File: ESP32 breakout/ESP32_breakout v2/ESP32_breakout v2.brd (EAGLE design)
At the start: 53.3 x 63.5 mm, 35 parts, among them U1 ESP-WROOM-32, U2 NCP-1117, Y1 12MHz

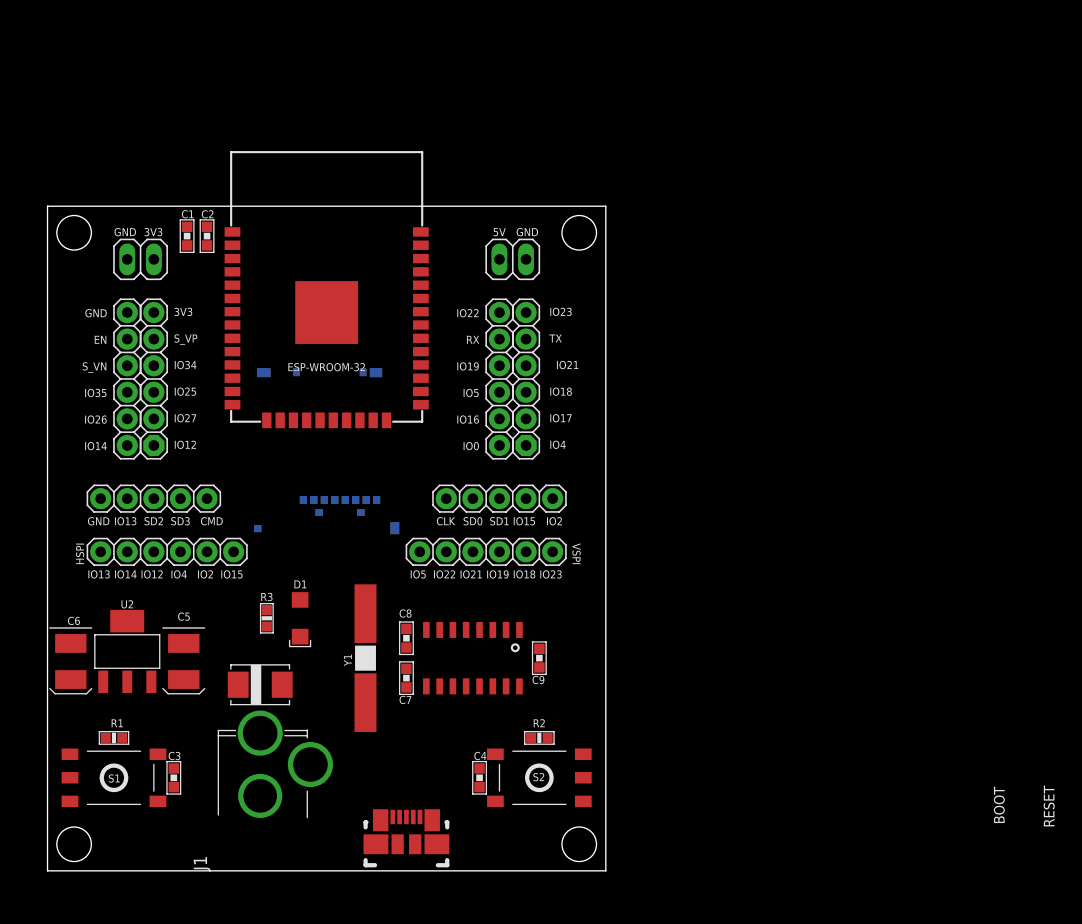
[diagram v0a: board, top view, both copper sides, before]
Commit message: Made rounded board. Modified component libraries
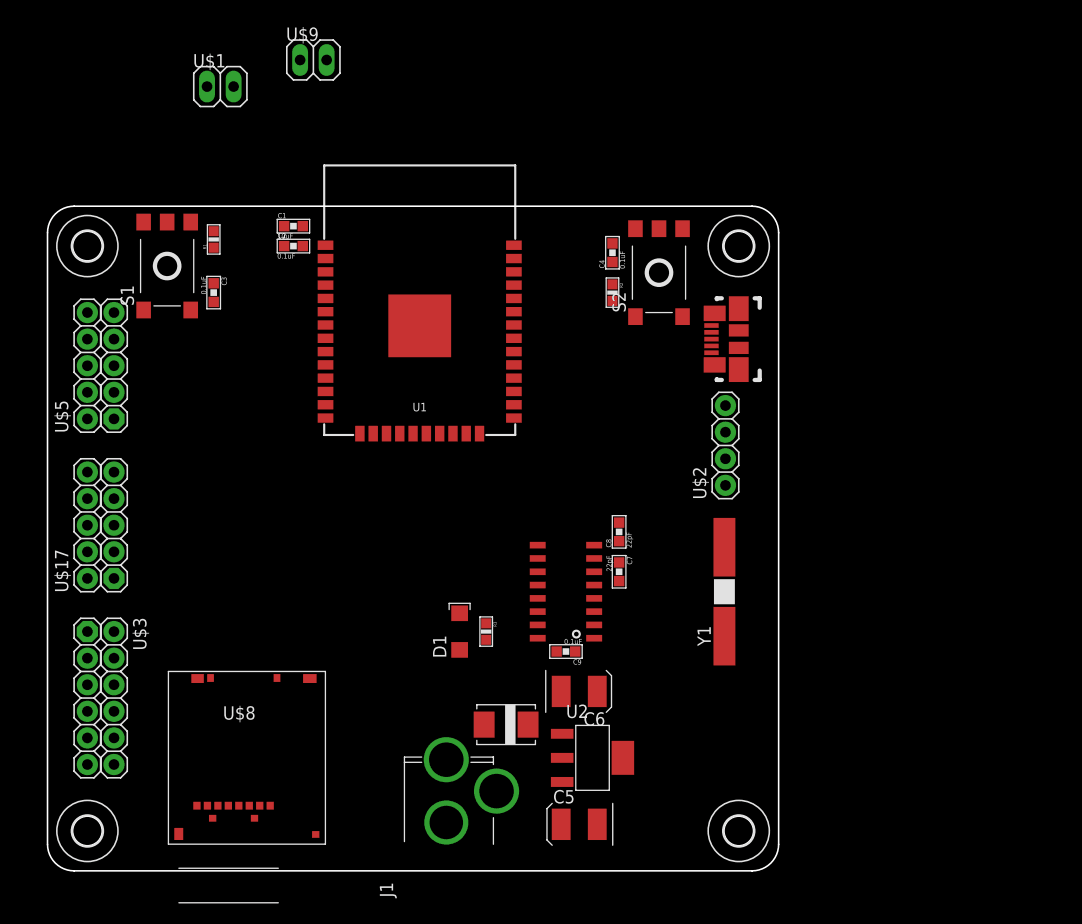
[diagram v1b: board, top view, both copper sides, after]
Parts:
- removed U$14, U$15: M05, dr-library:1X05
- removed U$6: M06, dr-library:1X06
- added U$17: M102X05, dr-library:2X05
- U$10, U$11, U$12, U$13: device EmbeddedAdventures 3:STAND-OFF-HOLE -> holes:2,8
- U$2: value M122ROWS -> M04; device dr-library:2X06 -> dr-library:1X04
- U$5: value M06 -> M102X05; device dr-library:1X06 -> dr-library:2X05
- moved U$13 85.4 mm to (66.0, 3.81)
- moved U$11 74.0 mm to (3.81, 59.7)
- moved U$4 57.8 mm to (66.0, 50.8), turned to 180 degrees
- moved U$2 57.3 mm to (64.8, 38.1)
- moved C4 51.7 mm to (54.0, 59.1)
- moved S2 49.6 mm to (58.4, 57.1), turned to 90 degrees
- moved S1 49.2 mm to (11.4, 57.8), turned to 90 degrees
- moved C6 48.7 mm to (50.8, 17.1), turned to 180 degrees
- moved R1 48.6 mm to (15.9, 60.3), turned to 90 degrees
- moved C3 46.5 mm to (15.9, 55.2)
- moved U2 45.6 mm to (52.1, 10.8), turned to 270 degrees
- moved R2 43.1 mm to (54.0, 55.2), turned to 270 degrees
- moved U$3 42.1 mm to (6.35, 21.6), turned to 270 degrees
- moved C5 40.9 mm to (50.8, 4.45), turned to 0 degrees
- moved U$5 35.9 mm to (3.81, 44.5), turned to 90 degrees
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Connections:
- net +3V3: now also U$2.4; no longer U$2.11
- net CLK: now also U$17.5; no longer U$14.1
- net CMD: now also U$17.6; no longer U$15.5
- net EN: now also S1.4, U$5.10; no longer U$2.10
- net GND: now also S1.2, S2.2, U$17.10, U$2.3; no longer J1.2, U$15.1, U$2.12
- net IO0: now also S2.4, U$3.1; no longer U$3.2
- net IO12: now also U$5.1; no longer U$2.1, U$6.4
- net IO13: now also U$17.9; no longer U$15.2, U$6.6
- net IO14: now also U$5.2; no longer U$2.2, U$6.5
- net IO15: now also U$17.2; no longer U$14.4, U$6.1
- net IO16: now also U$3.3; no longer U$3.4
- net IO17: now also U$3.4; no longer U$3.3
- net IO18: now also U$3.6; no longer U$3.5, U$5.5
- net IO19: now also U$3.7; no longer U$3.8, U$5.4
- net IO2: now also U$17.1; no longer U$14.5, U$6.2
- net IO21: now also U$3.8; no longer U$3.7, U$5.3
- net IO22: now also U$3.11; no longer U$3.12, U$5.2
- net IO23: now also U$3.12; no longer U$3.11, U$5.6
- net IO25: now also U$5.5; no longer U$2.5
- net IO26: now also U$5.4; no longer U$2.4
- net IO27: now also U$5.3; no longer U$2.3
- net IO34: now also U$5.7; no longer U$2.7
- net IO35: now also U$5.6; no longer U$2.6
- net IO4: now also U$3.2; no longer U$3.1, U$6.3
- net IO5: now also U$3.5; no longer U$3.6, U$5.1
- net RX: now also U$2.1, U$3.9, U$7.2; no longer U$3.10, U$7.3
- net SD0: now also U$17.4; no longer U$14.2
- net SD1: now also U$17.3; no longer U$14.3
- net SD2: now also U$17.8; no longer U$15.3
- net SD3: now also U$17.7; no longer U$15.4
- net S_VN: now also U$5.8; no longer U$2.8
- net S_VP: now also U$5.9; no longer U$2.9
- net TX: now also U$2.2, U$3.10, U$7.3; no longer U$3.9, U$7.2
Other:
- board size 53.3 x 63.5 mm -> 69.8 x 63.5 mm
- board text removed: "3V3"
- board text removed: "5V"
- board text removed: "BOOT"
- board text removed: "C6"
- board text removed: "CLK"
- board text removed: "CMD"
- board text removed: "DRances"
- board text removed: "EN"
- board text removed: "ESP32 Breaakout v1"
- board text removed: "GND"
- board text removed: "HSPI"
- board text removed: "IO0"
- board text removed: "IO12"
- board text removed: "IO13"
- board text removed: "IO14"
- board text removed: "IO15"
- board text removed: "IO16"
- board text removed: "IO17"
- board text removed: "IO18"
- board text removed: "IO19"
- board text removed: "IO2"
- board text removed: "IO21"
- board text removed: "IO22"
- board text removed: "IO23"
- board text removed: "IO25"
- board text removed: "IO26"
- board text removed: "IO27"
- board text removed: "IO34"
- board text removed: "IO35"
- board text removed: "IO4"
- board text removed: "IO5"
- board text removed: "May 15 2017"
- board text removed: "RESET"
- board text removed: "RX"
- board text removed: "SD0"
- board text removed: "SD1"
- board text removed: "SD2"
- board text removed: "SD3"
- board text removed: "S_VN"
- board text removed: "S_VP"
- board text removed: "TX"
- board text removed: "VSPI"

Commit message: Resized PCB v2
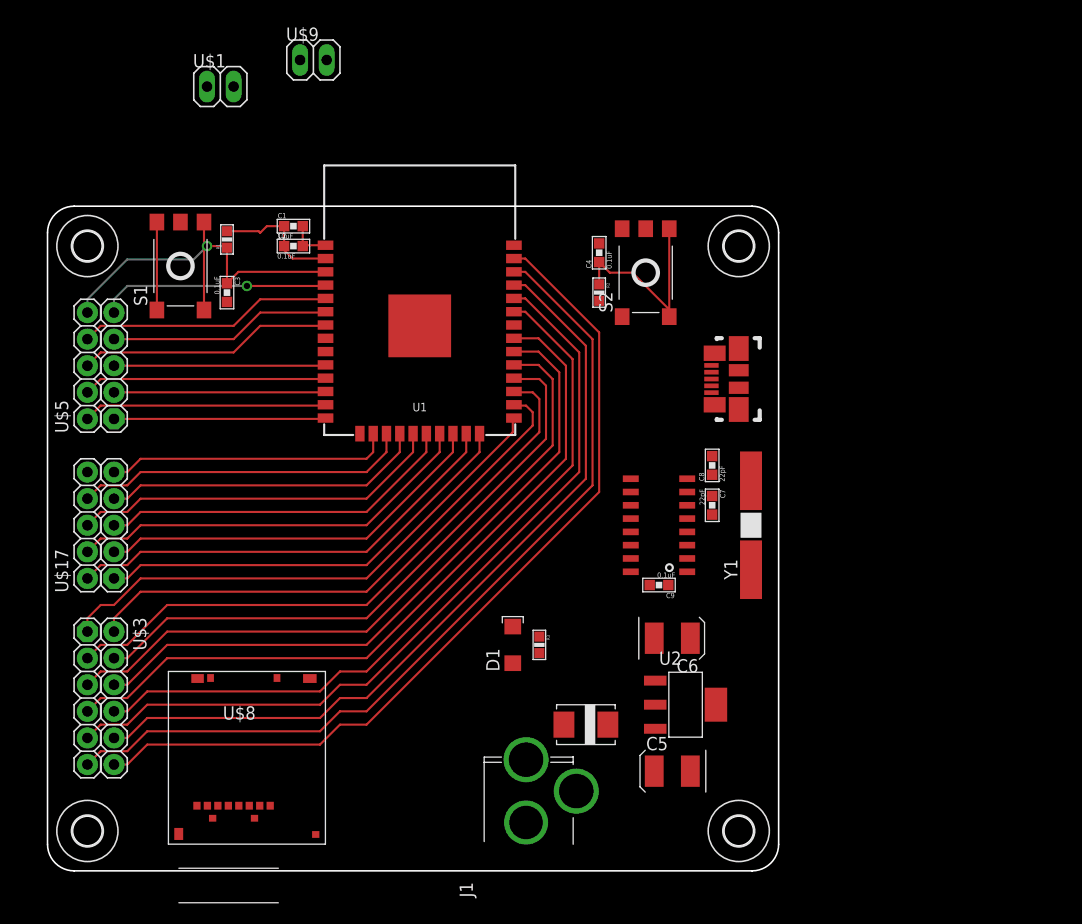
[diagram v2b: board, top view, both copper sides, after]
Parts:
- removed U$2: M04, dr-library:1X04
- moved C8 10.9 mm to (63.5, 38.7)
- moved C9 10.9 mm to (58.4, 27.3)
- moved U$7 10.9 mm to (58.4, 33.0)
- moved C7 10.9 mm to (63.5, 34.9)
- moved C5 10.2 mm to (59.7, 9.53)
- moved C6 10.2 mm to (59.7, 22.2)
- moved U2 10.2 mm to (61.0, 15.9)
- moved U$16 7.62 mm to (51.4, 14.0)
- moved J1 7.62 mm to (45.7, 7.62)
- moved Y1 6.84 mm to (67.3, 33.0)
- moved D1 5.24 mm to (44.5, 21.6)
- moved R3 5.24 mm to (47.0, 21.6)
- moved U$4 3.81 mm to (66.0, 47.0)
- moved C4 1.27 mm to (52.7, 59.1)
- moved R2 1.27 mm to (52.7, 55.2)
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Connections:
- net +3V3: no longer U$2.4
- net GND: no longer U$2.3
- net RX: no longer U$2.1
- net TX: no longer U$2.2
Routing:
- net IO22: track 0.00 -> 83.5 mm
- net IO23: track 0.00 -> 83.5 mm
- net TX: track 0.00 -> 77.3 mm
- net RX: track 0.00 -> 77.3 mm
- net IO21: track 0.00 -> 71.2 mm
- net IO19: track 0.00 -> 70.7 mm
- net IO0: track 0.00 -> 70.5 mm
- net IO5: track 0.00 -> 64.5 mm
- net IO18: track 0.00 -> 64.5 mm
- net IO17: track 0.00 -> 58.4 mm
- net IO16: track 0.00 -> 58.0 mm
- net IO4: track 0.00 -> 52.3 mm
- net IO15: track 0.00 -> 43.0 mm
- net IO2: track 0.00 -> 41.7 mm
- net SD0: track 0.00 -> 39.4 mm
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
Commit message: Finished major traces
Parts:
- removed U$11, U$12, U$13: (no value), holes:2,8
- added U$14, U$15, U$6: (no value), EmbeddedAdventures 3:STAND-OFF-HOLE
- added U$2: M102X05, dr-library:2X05
- U$10: value (none) -> M04; device holes:2,8 -> dr-library:1X04
- U$3: value M122ROWS -> (none); device dr-library:2X06 -> EmbeddedAdventures 3:STAND-OFF-HOLE
- moved U$9 75.8 mm to (43.2, 3.81), turned to 90 degrees
- moved U$10 73.0 mm to (66.0, 41.9), turned to 90 degrees
- moved U$1 72.5 mm to (30.5, 3.81), turned to 90 degrees
- moved U$3 32.0 mm to (2.54, 53.3), turned to 0 degrees
- moved C5 29.5 mm to (30.5, 14.0), turned to 270 degrees
- moved U2 24.3 mm to (36.8, 12.7), turned to 180 degrees
- moved C6 18.5 mm to (43.2, 14.0), turned to 90 degrees
- moved U$4 13.4 mm to (67.3, 33.7)
- moved Y1 12.1 mm to (67.3, 21.0)
- moved C7 12.1 mm to (63.5, 22.9)
- moved C8 12.1 mm to (63.5, 26.7)
- moved J1 11.5 mm to (57.1, 8.89)
- moved U$7 10.8 mm to (58.4, 22.2)
- moved C9 10.8 mm to (58.4, 16.5)
- moved R1 7.73 mm to (18.4, 52.7)
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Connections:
- net +3V3: now also U$10.4
- net GND: now also U$10.3
- net IO0: now also U$2.1; no longer U$3.1
- net IO16: now also U$2.3; no longer U$3.3
- net IO17: now also U$2.4; no longer U$3.4
- net IO18: now also U$2.6; no longer U$3.6
- net IO19: now also U$2.7; no longer U$3.7
- net IO21: now also U$2.8; no longer U$3.8
- net IO22: now also U$2.9; no longer U$3.11
- net IO23: now also U$2.10; no longer U$3.12
- net IO4: now also U$2.2; no longer U$3.2
- net IO5: now also U$2.5; no longer U$3.5
- net RX: now also U$10.1; no longer U$3.9
- net TX: now also U$10.2; no longer U$3.10
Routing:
- net +3V3: track 12.4 -> 41.0 mm
- net IO0: track 70.5 -> 96.6 mm, vias 0 -> 3
- net TX: track 77.3 -> 54.7 mm, vias 0 -> 3
- net RX: track 77.3 -> 55.0 mm, vias 0 -> 3
- net N$5: track 0.00 -> 19.2 mm
- net N$6: track 0.00 -> 16.4 mm
- net GND: track 12.5 -> 26.3 mm
- net N$3: track 0.00 -> 11.6 mm
- net N$4: track 0.00 -> 6.70 mm
- net IO23: track 83.5 -> 81.3 mm
- net IO22: track 83.5 -> 81.7 mm
- net IO4: track 52.3 -> 50.7 mm
- net S_VP: track 22.0 -> 20.5 mm
- net IO5: track 64.5 -> 66.0 mm
- net IO18: track 64.5 -> 66.0 mm
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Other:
- board size 69.8 x 63.5 mm -> 69.8 x 55.9 mm

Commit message: Version 2, pre-check
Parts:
- turned D1 to 0 degrees
- renumbered U$16 to D2
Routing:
- net +3V3: track 41.0 -> 208.8 mm, vias 0 -> 4
- net VCC: track 0.00 -> 71.3 mm, vias 0 -> 2
- net GND: track 26.3 -> 95.6 mm, vias 0 -> 101
- net SD2: track 31.0 -> 70.6 mm, vias 0 -> 1
- net CMD: track 34.6 -> 70.6 mm, vias 0 -> 1
- net SD3: track 29.8 -> 65.5 mm, vias 0 -> 1
- net SD0: track 38.2 -> 67.8 mm, vias 0 -> 1
- net CLK: track 33.3 -> 62.7 mm, vias 0 -> 1
- net SD1: track 36.9 -> 60.2 mm, vias 0 -> 1
- net N$2: track 0.00 -> 6.62 mm
- net N$1: track 0.00 -> 2.94 mm
- net IO0: track 96.6 -> 94.4 mm
- net IO35: track 23.6 -> 25.2 mm
- net IO17: track 59.8 -> 59.3 mm
- added copper zone on layer 1, net GND
- added copper zone on layer 16, net GND
- added copper zone on layer 1, net N$7
- added copper zone on layer 1, net VCC
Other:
- board outline removed
- board text added: "3V3"
- board text added: "BOOT"
- board text added: "CLK"
- board text added: "CMD"
- board text added: "D2"
- board text added: "EN"
- board text added: "GND"
- board text added: "IO0"
- board text added: "IO12"
- board text added: "IO13"
- board text added: "IO14"
- board text added: "IO15"
- board text added: "IO16"
- board text added: "IO17"
- board text added: "IO18"
- board text added: "IO19"
- board text added: "IO2"
- board text added: "IO21"
- board text added: "IO22"
- board text added: "IO23"
- board text added: "IO25"
- board text added: "IO26"
- board text added: "IO27"
- board text added: "IO34"
- board text added: "IO35"
- board text added: "IO4"
- board text added: "IO5"
- board text added: "RESET"
- board text added: "RX"
- board text added: "SD0"
- board text added: "SD1"
- board text added: "SD2"
- board text added: "SD3"
- board text added: "SVN"
- board text added: "SVP"
- board text added: "TX"
- board text added: "VCC"

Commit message: Added labels
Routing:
- net GND: vias 101 -> 102
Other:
- board text added: "U1"
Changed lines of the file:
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@@
 <setting verticaltext="up"/>
 </settings>
-<grid distance="0.05" unitdist="inch" unit="inch" style="lines" multiple="1" display="yes" altdistance="0.0125" altunitdist="inch" altunit="inch"/>
+<grid distance="0.05" unitdist="inch" unit="inch" style="lines" multiple="1" display="yes" altdistance="0.025" altunitdist="inch" altunit="inch"/>
 <layers>
 <layer number="1" name="Top" color="4" fill="1" visible="yes" active="yes"/>
@@
 <text x="11.7475" y="42.2275" size="1.27" layer="21" font="vector" ratio="20">RESET</text>
 <text x="54.9275" y="42.545" size="1.27" layer="21" font="vector" ratio="20">BOOT</text>
+<text x="56.515" y="27.305" size="0.762" layer="21" font="vector" ratio="20">U1</text>
 </plain>
 <attributes>
@@
 </polygon>
 <via x="13.0175" y="18.7325" extent="1-16" drill="0.6"/>
-<via x="12.7" y="24.13" extent="1-16" drill="0.6"/>
+<via x="12.065" y="24.13" extent="1-16" drill="0.6"/>
 <via x="31.75" y="49.53" extent="1-16" drill="0.6"/>
 <via x="33.02" y="49.53" extent="1-16" drill="0.6"/>
@@
 <via x="54.61" y="34.29" extent="1-16" drill="0.6"/>
 <via x="54.61" y="35.56" extent="1-16" drill="0.6"/>
+<via x="22.5425" y="17.78" extent="1-16" drill="0.6"/>
 </signal>
 <signal name="+3V3">
@@
 <contactref element="U$17" pad="2"/>
 <wire x1="3.81" y1="22.86" x2="5.08" y2="24.13" width="0.1778" layer="1"/>
-<wire x1="5.08" y1="24.13" x2="9.525" y2="24.13" width="0.1778" layer="1"/>
-<wire x1="9.525" y1="24.13" x2="13.97" y2="28.575" width="0.1778" layer="1"/>
-<wire x1="13.97" y1="28.575" x2="34.925" y2="28.575" width="0.1778" layer="1"/>
+<wire x1="5.08" y1="24.13" x2="6.985" y2="24.13" width="0.1778" layer="1"/>
+<wire x1="6.985" y1="24.13" x2="11.43" y2="28.575" width="0.1778" layer="1"/>
+<wire x1="11.43" y1="28.575" x2="34.925" y2="28.575" width="0.1778" layer="1"/>
 <wire x1="34.925" y1="28.575" x2="40.005" y2="33.655" width="0.1778" layer="1"/>
 <wire x1="40.005" y1="33.655" x2="40.005" y2="34.785" width="0.1778" layer="1"/>
@@
 <contactref element="U1" pad="24"/>
 <contactref element="U$17" pad="1"/>
-<wire x1="6.35" y1="22.86" x2="10.16" y2="22.86" width="0.1778" layer="1"/>
-<wire x1="10.16" y1="22.86" x2="15.24" y2="27.94" width="0.1778" layer="1"/>
-<wire x1="15.24" y1="27.94" x2="35.56" y2="27.94" width="0.1778" layer="1"/>
+<wire x1="6.35" y1="22.86" x2="6.985" y2="22.86" width="0.1778" layer="1"/>
+<wire x1="6.985" y1="22.86" x2="12.065" y2="27.94" width="0.1778" layer="1"/>
+<wire x1="12.065" y1="27.94" x2="35.56" y2="27.94" width="0.1778" layer="1"/>
 <wire x1="35.56" y1="27.94" x2="41.275" y2="33.655" width="0.1778" layer="1"/>
 <wire x1="41.275" y1="33.655" x2="41.275" y2="34.785" width="0.1778" layer="1"/>
@@
 <wire x1="51.435" y1="46.355" x2="46.275" y2="51.515" width="0.1778" layer="1"/>
 <wire x1="44.56" y1="51.515" x2="46.275" y2="51.515" width="0.1778" layer="1"/>
-<wire x1="24.13" y1="20.955" x2="22.86" y2="19.685" width="0.1778" layer="1"/>
-<wire x1="22.86" y1="19.685" x2="22.86" y2="16.51" width="0.1778" layer="1"/>
-<wire x1="22.86" y1="16.51" x2="16.51" y2="10.16" width="0.1778" layer="1"/>
+<wire x1="24.13" y1="20.955" x2="23.495" y2="20.32" width="0.1778" layer="1"/>
+<wire x1="23.495" y1="20.32" x2="23.495" y2="17.145" width="0.1778" layer="1"/>
+<wire x1="23.495" y1="17.145" x2="16.51" y2="10.16" width="0.1778" layer="1"/>
 </signal>
 <signal name="IO17">
@@
 <contactref element="U$8" pad="8"/>
 <contactref element="U$17" pad="3"/>
-<wire x1="6.35" y1="25.4" x2="8.89" y2="25.4" width="0.1778" layer="1"/>
-<wire x1="8.89" y1="25.4" x2="12.7" y2="29.21" width="0.1778" layer="1"/>
-<wire x1="12.7" y1="29.21" x2="34.29" y2="29.21" width="0.1778" layer="1"/>
+<wire x1="6.35" y1="25.4" x2="6.985" y2="25.4" width="0.1778" layer="1"/>
+<wire x1="6.985" y1="25.4" x2="10.795" y2="29.21" width="0.1778" layer="1"/>
+<wire x1="10.795" y1="29.21" x2="34.29" y2="29.21" width="0.1778" layer="1"/>
 <wire x1="34.29" y1="29.21" x2="38.735" y2="33.655" width="0.1778" layer="1"/>
 <wire x1="38.735" y1="33.655" x2="38.735" y2="34.785" width="0.1778" layer="1"/>
@@
 <contactref element="U$17" pad="4"/>
 <wire x1="3.81" y1="25.4" x2="5.08" y2="26.67" width="0.1778" layer="1"/>
-<wire x1="5.08" y1="26.67" x2="8.255" y2="26.67" width="0.1778" layer="1"/>
-<wire x1="8.255" y1="26.67" x2="11.43" y2="29.845" width="0.1778" layer="1"/>
-<wire x1="11.43" y1="29.845" x2="33.655" y2="29.845" width="0.1778" layer="1"/>
+<wire x1="5.08" y1="26.67" x2="6.985" y2="26.67" width="0.1778" layer="1"/>
+<wire x1="6.985" y1="26.67" x2="10.16" y2="29.845" width="0.1778" layer="1"/>
+<wire x1="10.16" y1="29.845" x2="33.655" y2="29.845" width="0.1778" layer="1"/>
 <wire x1="33.655" y1="29.845" x2="37.465" y2="33.655" width="0.1778" layer="1"/>
 <wire x1="37.465" y1="33.655" x2="37.465" y2="34.785" width="0.1778" layer="1"/>
@@
 <contactref element="U$8" pad="5"/>
 <contactref element="U$17" pad="5"/>
-<wire x1="6.35" y1="27.94" x2="7.62" y2="27.94" width="0.1778" layer="1"/>
-<wire x1="7.62" y1="27.94" x2="10.16" y2="30.48" width="0.1778" layer="1"/>
-<wire x1="10.16" y1="30.48" x2="33.02" y2="30.48" width="0.1778" layer="1"/>
+<wire x1="6.35" y1="27.94" x2="6.985" y2="27.94" width="0.1778" layer="1"/>
+<wire x1="6.985" y1="27.94" x2="9.525" y2="30.48" width="0.1778" layer="1"/>
+<wire x1="9.525" y1="30.48" x2="33.02" y2="30.48" width="0.1778" layer="1"/>
 <wire x1="33.02" y1="30.48" x2="36.195" y2="33.655" width="0.1778" layer="1"/>
 <wire x1="36.195" y1="33.655" x2="36.195" y2="34.785" width="0.1778" layer="1"/>
